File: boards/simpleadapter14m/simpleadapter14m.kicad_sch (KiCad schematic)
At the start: 2 parts, among them J1 692112030100, J2 Conn_02x05_Odd_Even

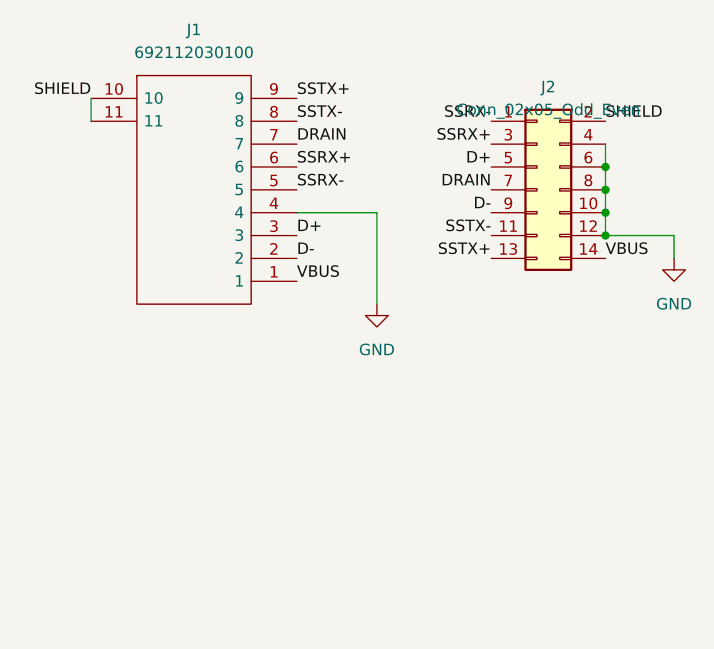
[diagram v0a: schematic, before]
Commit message: Move to 14 pin headers for switch with off-board adapters
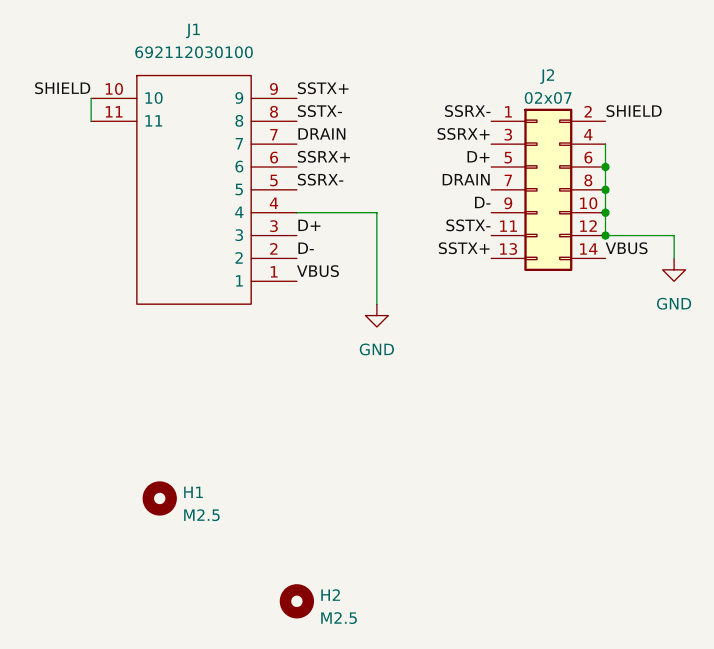
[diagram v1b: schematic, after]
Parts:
- added H1, H2: M2.5, MountingHole:MountingHole_2.7mm_M2.5, symbol Mechanical:MountingHole
- J2: value Conn_02x05_Odd_Even -> 02x07
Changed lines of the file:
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@@
     (pin "9")
     (instances
-      (project "simpleadapter14"
+      (project "simpleadapter14m"
         (path "/8982432f-a660-42bc-9ec2-b788d20f911f"
           (reference "J1") (unit 1)
@@
     )
   )
+  (symbol (lib_id "Mechanical:MountingHole") (at 96.52 127 0) (unit 1)
+    (in_bom yes) (on_board yes) (dnp no) (fields_autoplaced)
+    (property "Reference" "H2" (at 99.06 126.365 0)
+      (effects (font (size 1.27 1.27)) (justify left))
+    )
+    (property "Value" "M2.5" (at 99.06 128.905 0)
+      (effects (font (size 1.27 1.27)) (justify left))
+    )
+    (property "Footprint" "MountingHole:MountingHole_2.7mm_M2.5" (at 96.52 127 0)
+      (effects (font (size 1.27 1.27)) hide)
+    )
+    (property "Datasheet" "~" (at 96.52 127 0)
+      (effects (font (size 1.27 1.27)) hide)
+    )
+    (instances
+      (project "simpleadapter14m"
+        (path "/8982432f-a660-42bc-9ec2-b788d20f911f"
+          (reference "H2") (unit 1)
+        )
+      )
+    )
+  )
   (symbol (lib_id "Connector_Generic:Conn_02x07_Odd_Even") (at 123.19 81.28 0) (unit 1)
     (in_bom yes) (on_board yes) (dnp no) (fields_autoplaced)
-    (property "Reference" "J2" (at 124.46 69.85 0)
+    (property "Reference" "J2" (at 124.46 68.58 0)
       (effects (font (size 1.27 1.27)))
     )
-    (property "Value" "Conn_02x05_Odd_Even" (at 124.46 72.39 0)
+    (property "Value" "02x07" (at 124.46 71.12 0)
       (effects (font (size 1.27 1.27)))
     )
@@
     (pin "9")
     (instances
-      (project "simpleadapter14"
+      (project "simpleadapter14m"
         (path "/8982432f-a660-42bc-9ec2-b788d20f911f"
           (reference "J2") (unit 1)
@@
     (pin "1")
     (instances
-      (project "simpleadapter14"
+      (project "simpleadapter14m"
         (path "/8982432f-a660-42bc-9ec2-b788d20f911f"
           (reference "#PWR02") (unit 1)
+        )
+      )
+    )
+  )
+  (symbol (lib_id "Mechanical:MountingHole") (at 81.28 115.57 0) (unit 1)
+    (in_bom yes) (on_board yes) (dnp no) (fields_autoplaced)
+    (property "Reference" "H1" (at 83.82 114.935 0)
+      (effects (font (size 1.27 1.27)) (justify left))
+    )
+    (property "Value" "M2.5" (at 83.82 117.475 0)
+      (effects (font (size 1.27 1.27)) (justify left))
+    )
+    (property "Footprint" "MountingHole:MountingHole_2.7mm_M2.5" (at 81.28 115.57 0)
+      (effects (font (size 1.27 1.27)) hide)
+    )
+    (property "Datasheet" "~" (at 81.28 115.57 0)
+      (effects (font (size 1.27 1.27)) hide)
+    )
+    (instances
+      (project "simpleadapter14m"
+        (path "/8982432f-a660-42bc-9ec2-b788d20f911f"
+          (reference "H1") (unit 1)
         )
       )
@@
     (pin "1")
     (instances
-      (project "simpleadapter14"
+      (project "simpleadapter14m"
         (path "/8982432f-a660-42bc-9ec2-b788d20f911f"
           (reference "#PWR01") (unit 1)
